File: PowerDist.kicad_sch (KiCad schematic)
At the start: 20 parts, among them J18 PowerConn, U12 RI3-1205S, U13 NCP1117-3.3_SOT223, U16 RI3-1212S

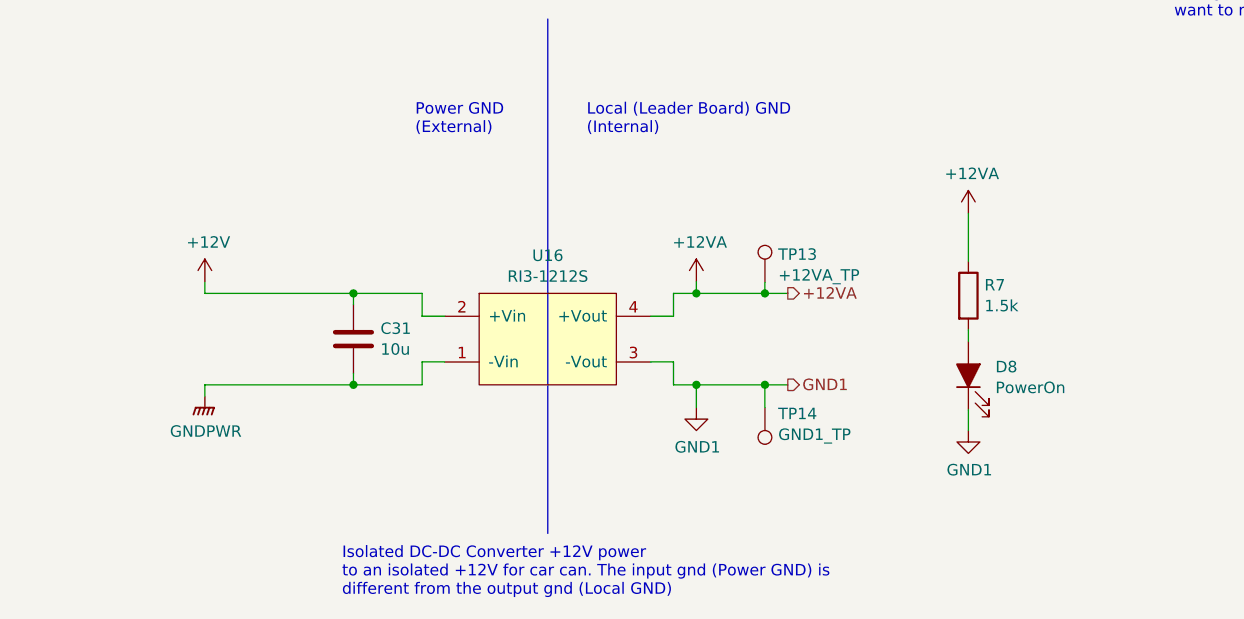
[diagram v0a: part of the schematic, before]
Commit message: Remove 12V isolator, swap CAN connector pins, etc.
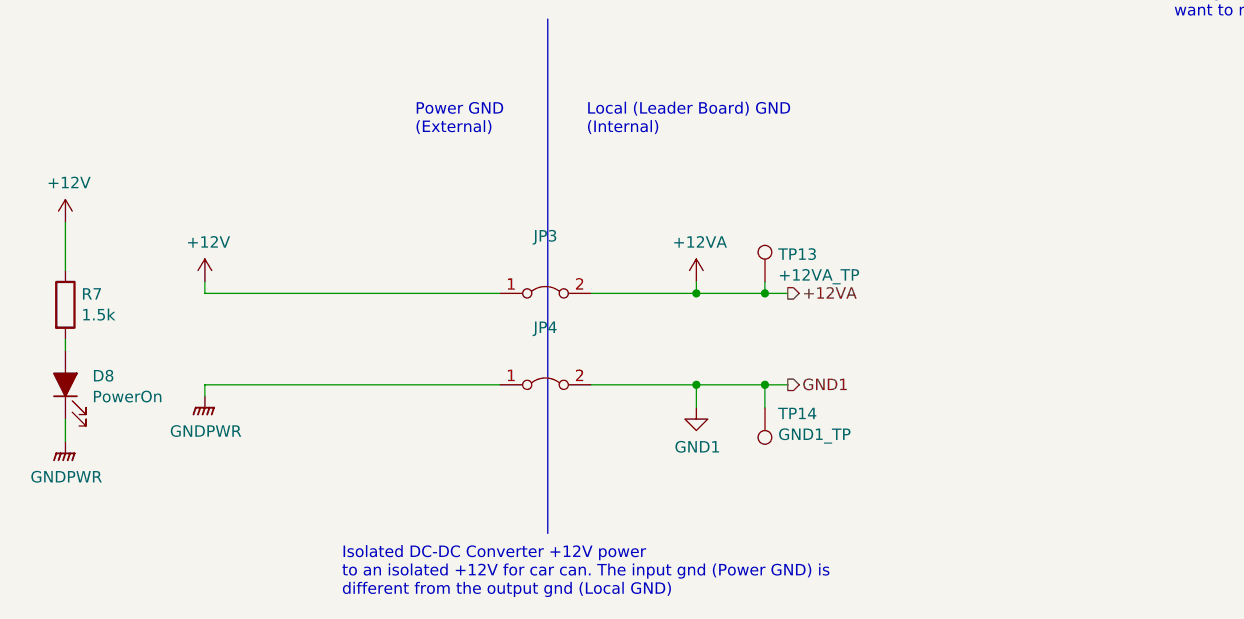
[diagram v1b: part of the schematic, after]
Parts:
- removed C31: 10u, UTSVT_Passive:C_2220_5750Metric, symbol Device:C
- removed U16: RI3-1212S, UTSVT_ICs:RI3_DC_Converter, symbol Dashboard-rescue:RI3-1205S-utsvt-power-regulators
- added JP3, JP4: (no value), symbol Jumper:Jumper_2_Bridged
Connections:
- net +12V: now also R7.1, JP3.1 (A)
- net +12VA: now also JP3.2 (B); no longer R7.1
- net GND1: now also JP4.2 (B); no longer D8.1 (K)
- net GNDPWR: now also D8.1 (K), JP4.1 (A)
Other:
- moved on the sheet: D8, R7

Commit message: Release v2.4 and gerbers
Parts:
- JP3, JP4: value (none) -> Jumper_2_Bridged; footprint (none) -> Jumper:SolderJumper-2_P1.3mm_Open_Pad1.0x1.5mm
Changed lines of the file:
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@@
     (in_bom yes) (on_board yes) (fields_autoplaced)
     (property "Reference" "JP3" (id 0) (at 113.03 143.51 0))
-    (property "Value" "" (id 1) (at 113.03 146.05 0))
-    (property "Footprint" "" (id 2) (at 113.03 149.86 0)
+    (property "Value" "Jumper_2_Bridged" (id 1) (at 113.03 146.05 0))
+    (property "Footprint" "Jumper:SolderJumper-2_P1.3mm_Open_Pad1.0x1.5mm" (id 2) (at 113.03 149.86 0)
       (effects (font (size 1.27 1.27)) hide)
     )
@@
     (in_bom yes) (on_board yes) (fields_autoplaced)
     (property "Reference" "JP4" (id 0) (at 113.03 153.67 0))
-    (property "Value" "" (id 1) (at 113.03 156.21 0))
-    (property "Footprint" "" (id 2) (at 113.03 160.02 0)
+    (property "Value" "Jumper_2_Bridged" (id 1) (at 113.03 156.21 0))
+    (property "Footprint" "Jumper:SolderJumper-2_P1.3mm_Open_Pad1.0x1.5mm" (id 2) (at 113.03 160.02 0)
       (effects (font (size 1.27 1.27)) hide)
     )

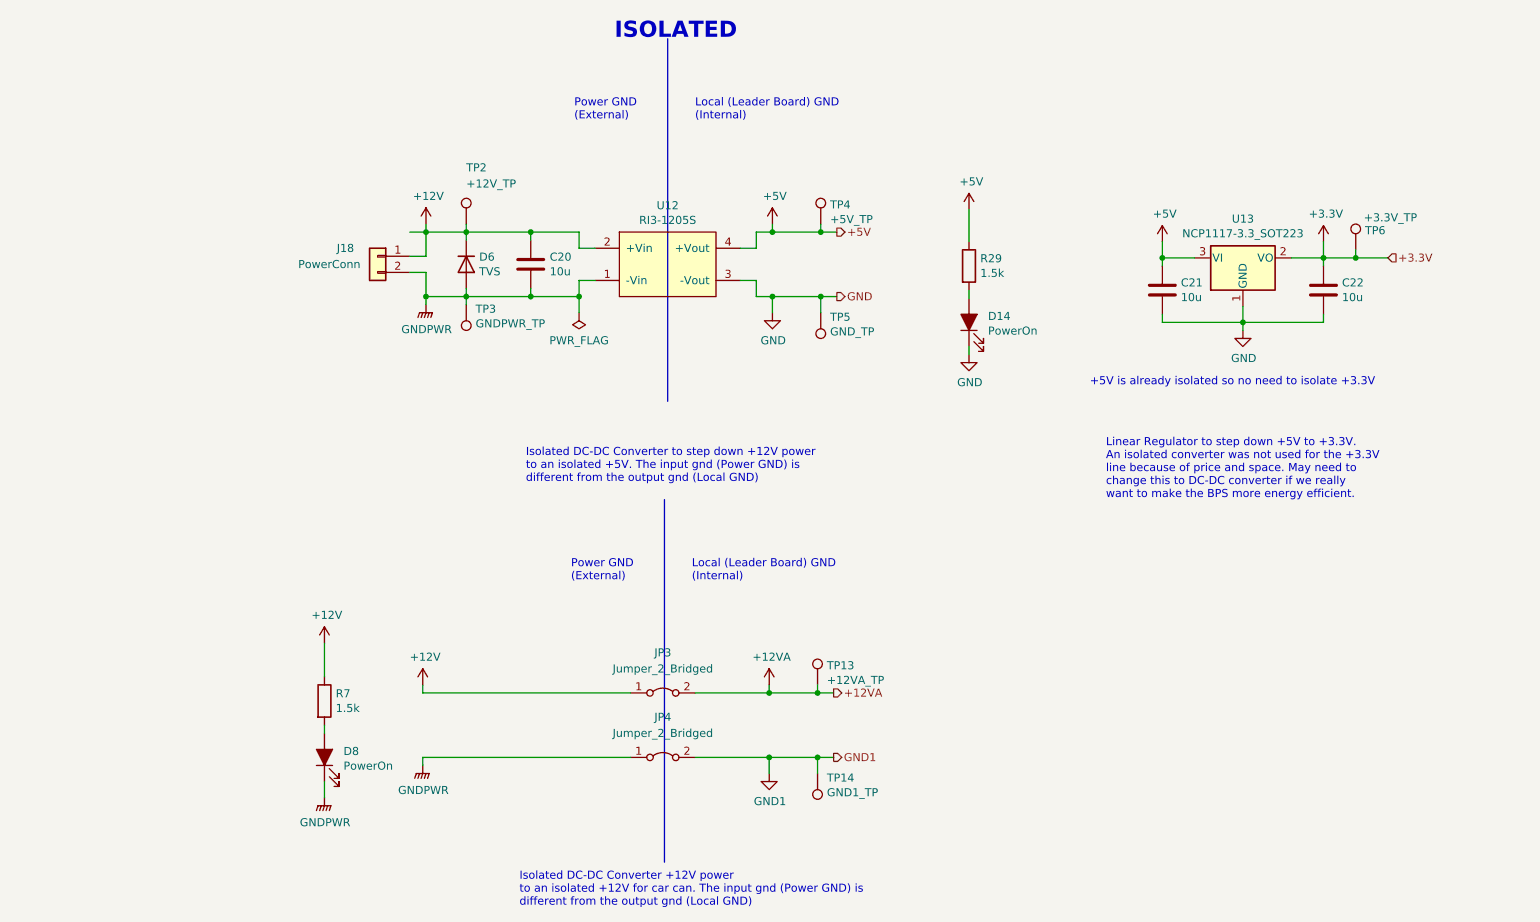
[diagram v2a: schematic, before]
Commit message: Schematic notations for rework changes
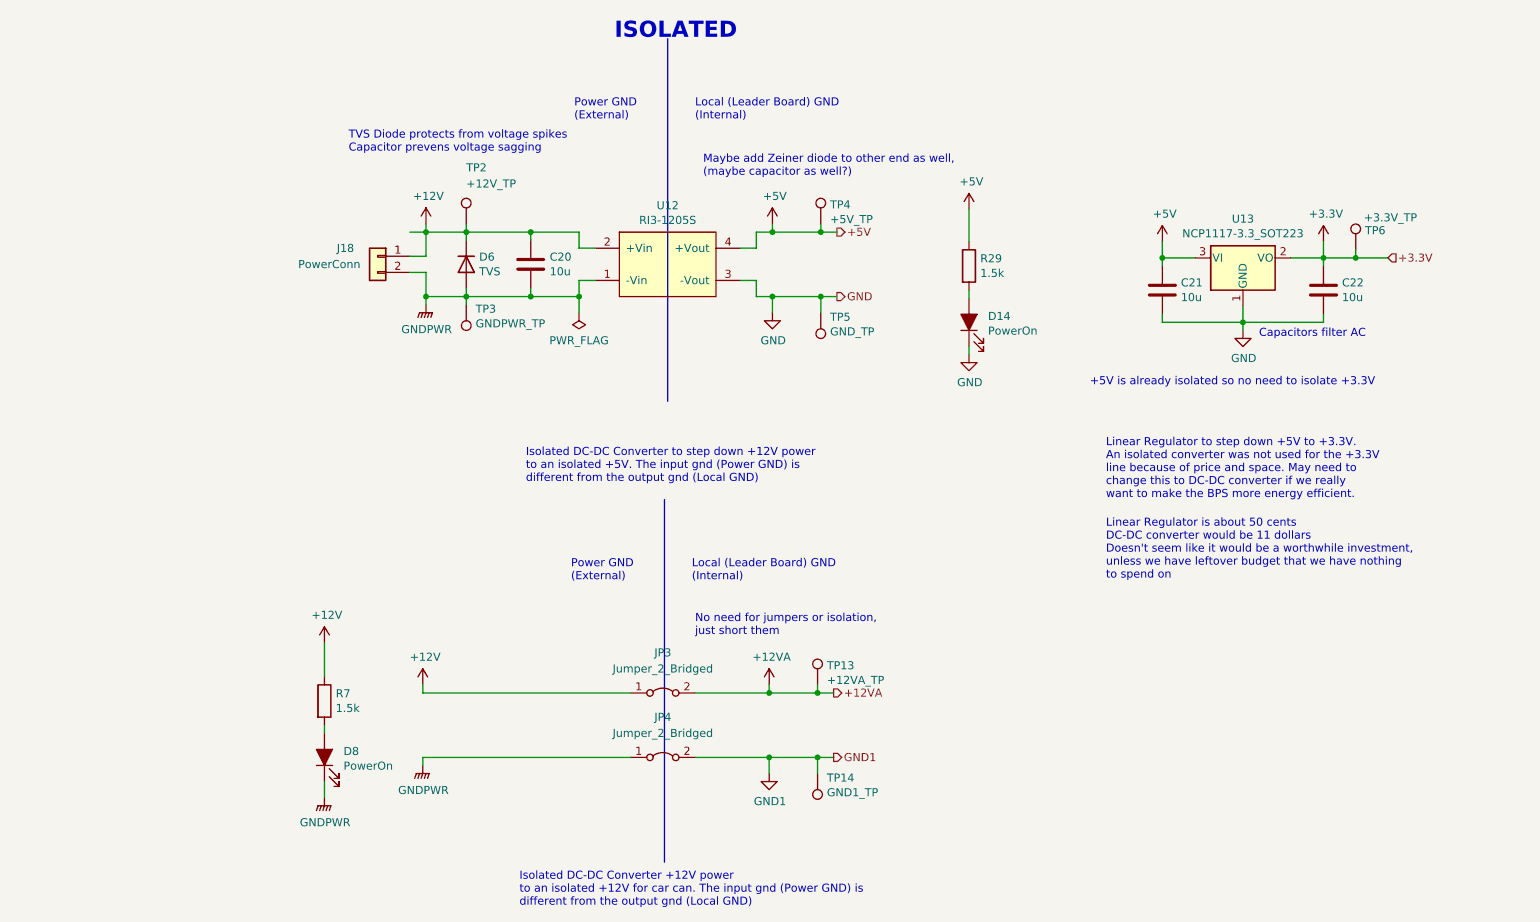
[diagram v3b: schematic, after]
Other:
- note added: "Capacitors filter AC"
- note added: "Linear Regulator is about 50 cents DC-DC converter would be 11 dollars Doesn't seem like it would be a worthwhile investment, unless we have leftover budget that we have nothing to spend on"
- note added: "Maybe add Zeiner diode to other end as well, (maybe capacitor as well?)"
- note added: "No need for jumpers or isolation, just short them"
- note added: "TVS Diode protects from voltage spikes Capacitor prevens voltage sagging"

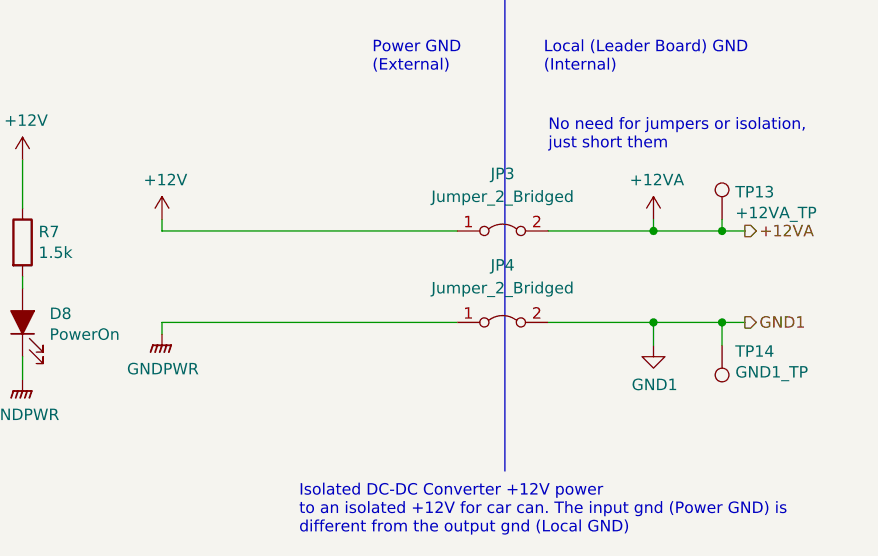
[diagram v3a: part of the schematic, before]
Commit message: Updated schematic in accordance to previous weeks annotated changes
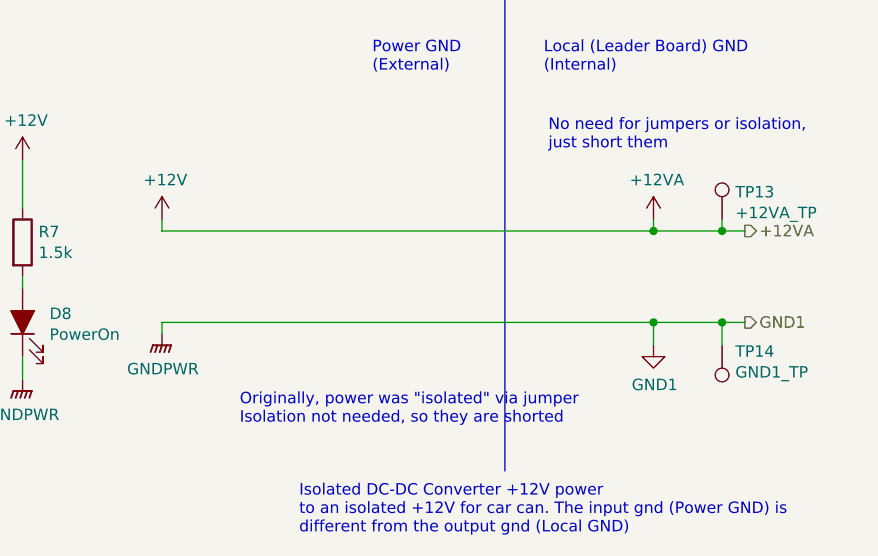
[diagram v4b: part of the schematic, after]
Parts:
- removed JP3, JP4: Jumper_2_Bridged, Jumper:SolderJumper-2_P1.3mm_Open_Pad1.0x1.5mm, symbol Jumper:Jumper_2_Bridged
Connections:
- net +12VA is gone; now on net +12V: TP13.1
- net GNDPWR is gone; now on net GND1: C20.2, D6.2 (A), D8.1 (K), J18.2 (Pin_2), TP3.1, U12.1 (-Vin)
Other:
- note added: "Originally, power was "isolated" via jumper Isolation not needed, so they are shorted"
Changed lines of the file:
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@@
     (stroke (width 0) (type default))
   )
-  (wire (pts (xy 118.11 149.86) (xy 129.794 149.86))
+  (wire (pts (xy 75.184 149.86) (xy 129.794 149.86))
     (stroke (width 0) (type default))
   )
@@
     (stroke (width 0) (type default))
   )
-  (wire (pts (xy 75.184 160.02) (xy 107.95 160.02))
-    (stroke (width 0) (type default))
-  )
-  (wire (pts (xy 118.11 160.02) (xy 129.794 160.02))
+  (wire (pts (xy 75.184 160.02) (xy 129.794 160.02))
     (stroke (width 0) (type default))
   )
@@
   )
   (wire (pts (xy 99.822 87.376) (xy 99.822 89.916))
-    (stroke (width 0) (type default))
-  )
-  (wire (pts (xy 75.184 149.86) (xy 107.95 149.86))
     (stroke (width 0) (type default))
   )
@@
     (effects (font (size 1.27 1.27) (color 255 0 15 1)) (justify left bottom))
   )
+  (text "Originally, power was \"isolated\" via jumper\nIsolation not needed, so they are shorted\n"
+    (at 83.82 171.45 0)
+    (effects (font (size 1.27 1.27) (color 255 0 11 1)) (justify left bottom))
+  )
   (text "Linear Regulator to step down +5V to +3.3V.\nAn isolated converter was not used for the +3.3V\nline because of price and space. May need to\nchange this to DC-DC converter if we really\nwant to make the BPS more energy efficient."
     (at 182.88 119.38 0)
@@
     )
   )
-  (symbol (lib_id "Jumper:Jumper_2_Bridged") (at 113.03 149.86 0) (unit 1)
-    (in_bom yes) (on_board yes) (dnp no) (fields_autoplaced)
-    (property "Reference" "JP3" (at 113.03 143.51 0)
-      (effects (font (size 1.27 1.27)))
-    )
-    (property "Value" "Jumper_2_Bridged" (at 113.03 146.05 0)
-      (effects (font (size 1.27 1.27)))
-    )
-    (property "Footprint" "Jumper:SolderJumper-2_P1.3mm_Open_Pad1.0x1.5mm" (at 113.03 149.86 0)
-      (effects (font (size 1.27 1.27)) hide)
-    )
-    (property "Datasheet" "~" (at 113.03 149.86 0)
-      (effects (font (size 1.27 1.27)) hide)
-    )
-    (pin "1")
-    (pin "2")
-    (instances
-      (project "Controls-Leader"
-        (path "/66218487-e316-4467-9eba-79d4626ab24e/00000000-0000-0000-0000-00005f19a9c5"
-          (reference "JP3") (unit 1)
-        )
-      )
-    )
-  )
   (symbol (lib_id "power:+12V") (at 59.69 141.986 0) (unit 1)
     (in_bom yes) (on_board yes) (dnp no)
-    (property "Reference" "#PWR?" (at 59.69 145.796 0)
+    (property "Reference" "#PWR0112" (at 59.69 145.796 0)
       (effects (font (size 1.27 1.27)) hide)
     )
@@
       (project "Controls-Leader"
         (path "/66218487-e316-4467-9eba-79d4626ab24e/00000000-0000-0000-0000-00005f19a9c5"
-          (reference "#PWR?") (unit 1)
+          (reference "#PWR0112") (unit 1)
         )
       )
@@
   (symbol (lib_id "power:GNDPWR") (at 59.69 166.37 0) (unit 1)
     (in_bom yes) (on_board yes) (dnp no)
-    (property "Reference" "#PWR?" (at 59.69 171.45 0)
+    (property "Reference" "#PWR0111" (at 59.69 171.45 0)
       (effects (font (size 1.27 1.27)) hide)
     )
@@
       (project "Controls-Leader"
         (path "/66218487-e316-4467-9eba-79d4626ab24e/00000000-0000-0000-0000-00005f19a9c5"
-          (reference "#PWR?") (unit 1)
-        )
-      )
-    )
-  )
-  (symbol (lib_id "Jumper:Jumper_2_Bridged") (at 113.03 160.02 0) (unit 1)
-    (in_bom yes) (on_board yes) (dnp no) (fields_autoplaced)
-    (property "Reference" "JP4" (at 113.03 153.67 0)
-      (effects (font (size 1.27 1.27)))
-    )
-    (property "Value" "Jumper_2_Bridged" (at 113.03 156.21 0)
-      (effects (font (size 1.27 1.27)))
-    )
-    (property "Footprint" "Jumper:SolderJumper-2_P1.3mm_Open_Pad1.0x1.5mm" (at 113.03 160.02 0)
-      (effects (font (size 1.27 1.27)) hide)
-    )
-    (property "Datasheet" "~" (at 113.03 160.02 0)
-      (effects (font (size 1.27 1.27)) hide)
-    )
-    (pin "1")
-    (pin "2")
-    (instances
-      (project "Controls-Leader"
-        (path "/66218487-e316-4467-9eba-79d4626ab24e/00000000-0000-0000-0000-00005f19a9c5"
-          (reference "JP4") (unit 1)
-        )
-      )
+          (reference "#PWR0111") (unit 1)
+        )
+      )

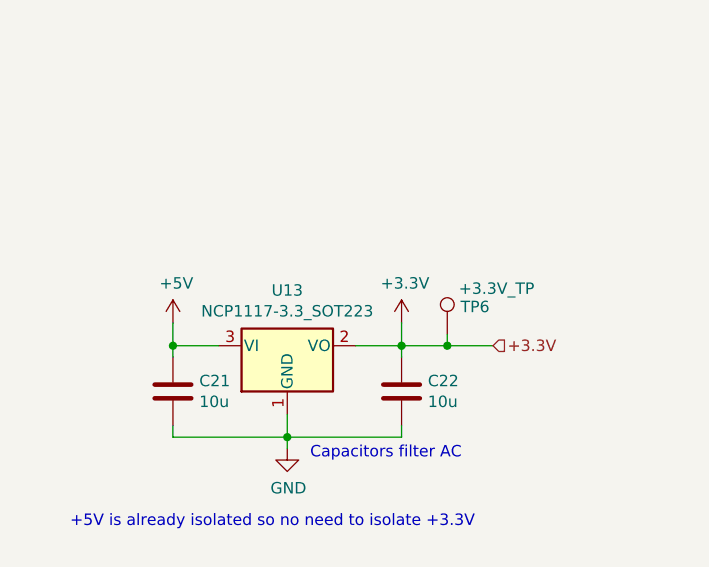
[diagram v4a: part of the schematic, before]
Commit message: Renamed Clk to PA5, removed CAN_TX/RX test points, deleted other .lck file and #auto_saved_files# (hopefully this does not break anything.
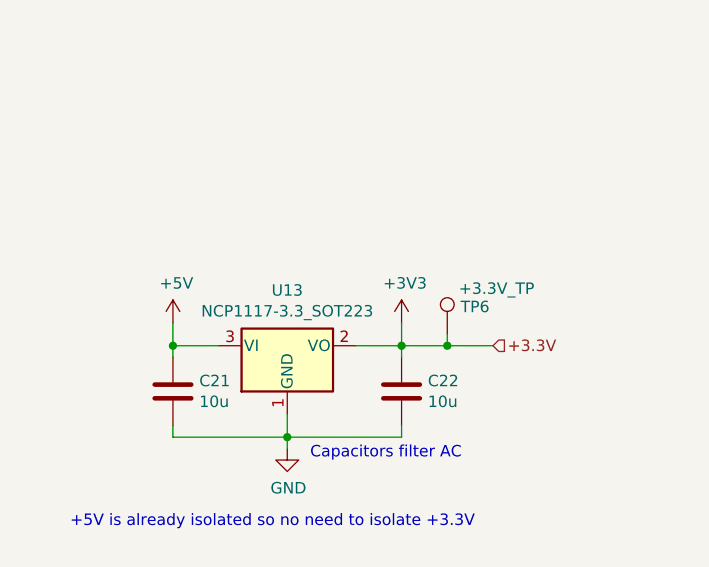
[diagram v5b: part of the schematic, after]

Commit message: Schematic finished :) hopefully not broken
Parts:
- removed TP13: +12VA_TP, TestPoint:TestPoint_Pad_1.5x1.5mm, symbol Connector:TestPoint
- removed TP14: GND1_TP, TestPoint:TestPoint_Pad_1.5x1.5mm, symbol Connector:TestPoint
- added Q1: NMOS, symbol Simulation_SPICE:NMOS
- added R_Gate1: R_US, symbol Device:R_US
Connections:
- net +12V: now also R_Gate1.1
- net GND1: no longer names the net of C20.2, D6.2 (A), TP3.1, U12.1 (-Vin)
- net GND1: now also Q1.1 (D); no longer D8.1 (K), J18.2 (Pin_2)
- new net: Q1.2 (G), R_Gate1.2
- new net GNDPWR: D8.1 (K), J18.2 (Pin_2), Q1.3 (S)
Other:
- note added: "Originally, GNDPWR and 12V was shorted to 12VA and GND1 Since they are the same, this shorting was removed and 12V and GNDPWR will be used in place of GND1 and 12VA"
- note added: "Reverse Polarity Protection If connected properly, Vgs = 12, nmos turns on, life is good If connected wrong, Vgs = -12, nmos turns off, no bueno"
- note removed: "No need for jumpers or isolation, just short them"
- note removed: "Originally, power was "isolated" via jumper Isolation not needed, so they are shorted"
- moved on the sheet: C20, D6, J18, TP2, TP3, TP4, TP5, U12
